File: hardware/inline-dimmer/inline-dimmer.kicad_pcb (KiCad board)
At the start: 2 copper layers, 42 x 13.6 mm, 15 parts, among them J1 Conn_01x01, J2 Conn_01x01, J3 1984633, J4 M5, J5 M5, Q2 DMP3013SFV, U1 MIC1555YM5-TR

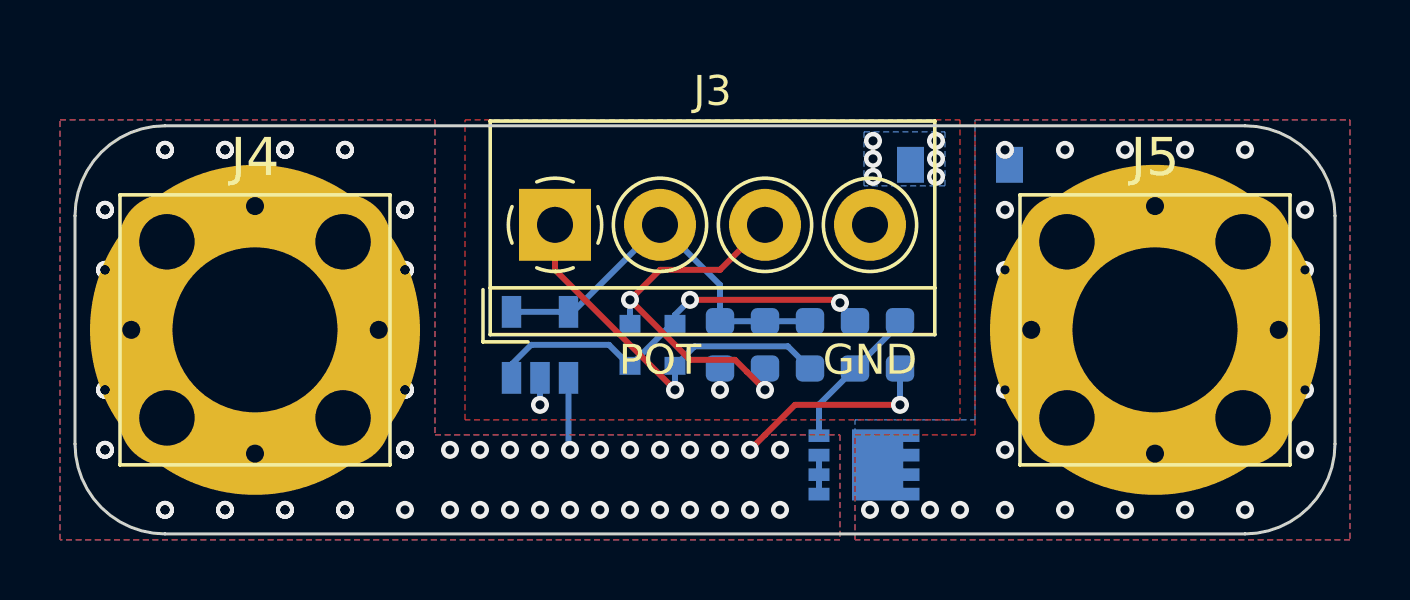
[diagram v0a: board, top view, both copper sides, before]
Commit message: Added silkscreen and LED
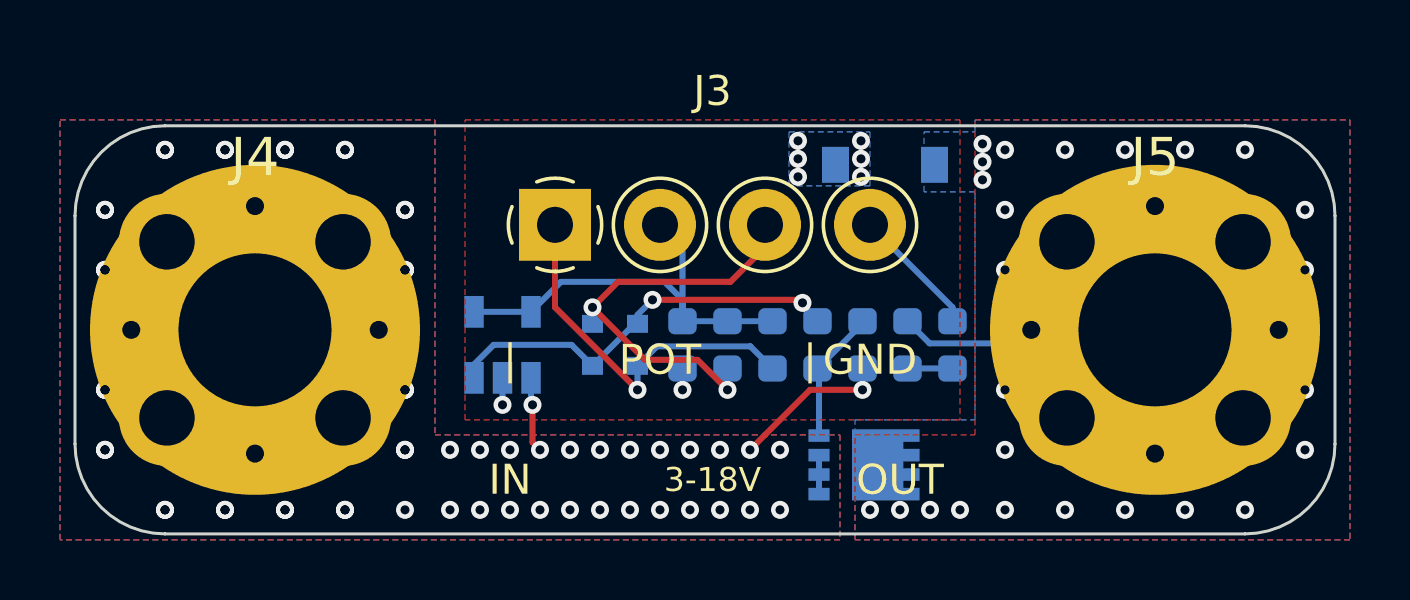
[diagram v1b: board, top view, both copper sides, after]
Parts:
- added D1: LED, LED_SMD:LED_0603_1608Metric, B.Cu at (158.2, 100.5)
- added R1: 2k, Resistor_SMD:R_0603_1608Metric, B.Cu at (156.8, 100.5)
- J4, J5: value M5 -> 74651175R
- moved D5 2.50 mm to (156.0, 94.5)
- moved C3 1.25 mm to (149.2, 100.5)
- moved D2 1.25 mm to (147.8, 100.5)
- moved D3 1.25 mm to (146.2, 100.5)
- moved R10 1.25 mm to (153.8, 100.5)
- moved R7 1.25 mm to (152.2, 100.5)
- moved R8 1.25 mm to (150.8, 100.5)
- moved R9 1.25 mm to (155.2, 100.5)
- moved U1 1.25 mm to (143.2, 100.5)
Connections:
- Q2 pad 1: +12V -> Net-(Q2-Pad1)
- Q2 pad 2: +12V -> Net-(Q2-Pad1)
- Q2 pad 3: +12V -> Net-(Q2-Pad1)
- Q2 pad 4: /GATE -> Net-(Q2-Pad4)
- Q2 pad 5: /LED_OUT -> Net-(Q2-Pad5)
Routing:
- net /LED_OUT: track 0.00 -> 8.74 mm, vias 22 -> 25
- net GND: track 1.61 -> 5.96 mm
- net +12V: track 10.6 -> 7.89 mm, vias 58 -> 59
- net /TRG_THR: track 13.2 -> 15.0 mm
- net Net-(D1-Pad2): track 0.00 -> 1.50 mm
- net Net-(D3-Pad2): track 12.8 -> 14.2 mm
- net Net-(Q2-Pad1): track 0.00 -> 1.30 mm
- net Net-(D2-Pad1): track 13.0 -> 12.5 mm
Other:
- board text added: "21.05.16 Rev 1"
- board text added: "3-18V"
- board text added: "IN"
- board text added: "OUT"
- board text added: "|"
